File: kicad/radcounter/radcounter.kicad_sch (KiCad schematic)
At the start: 34 parts, among them J1 SiPM(+), J2 SiPM(-), J3 Out, J4 Conn, J5 Conn, J6 Conn, Q2 RUM002N05T2L, T1 ATB322515-0110-T000, U2 MAX9120EXK

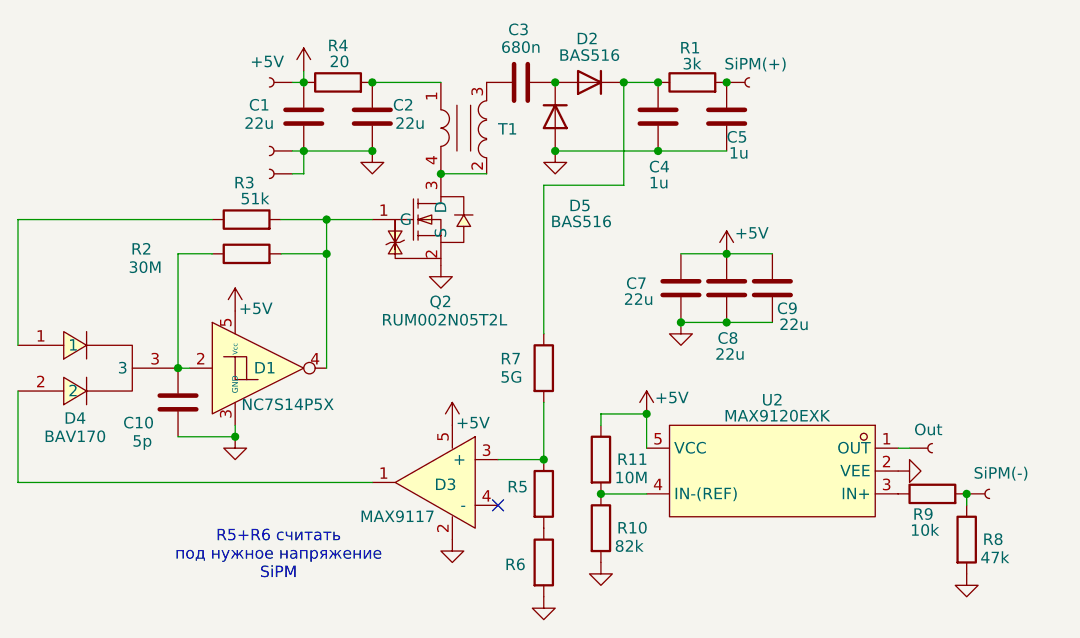
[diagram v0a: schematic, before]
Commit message: удалено:       kicad/radcounter/radcounter-backups/radcounter-2025-12-29_171823.zip 	удалено:       kicad/radcounter/radcounter-backups/radcounter-2026-01-03_121429.zip 	изменено:      kicad/radcounter/radcounter.kicad_pcb 	изменено:      kicad/radcounter/radcounter.kicad_prl 	изменено:      kicad/radcounter/radcounter.kicad_sch
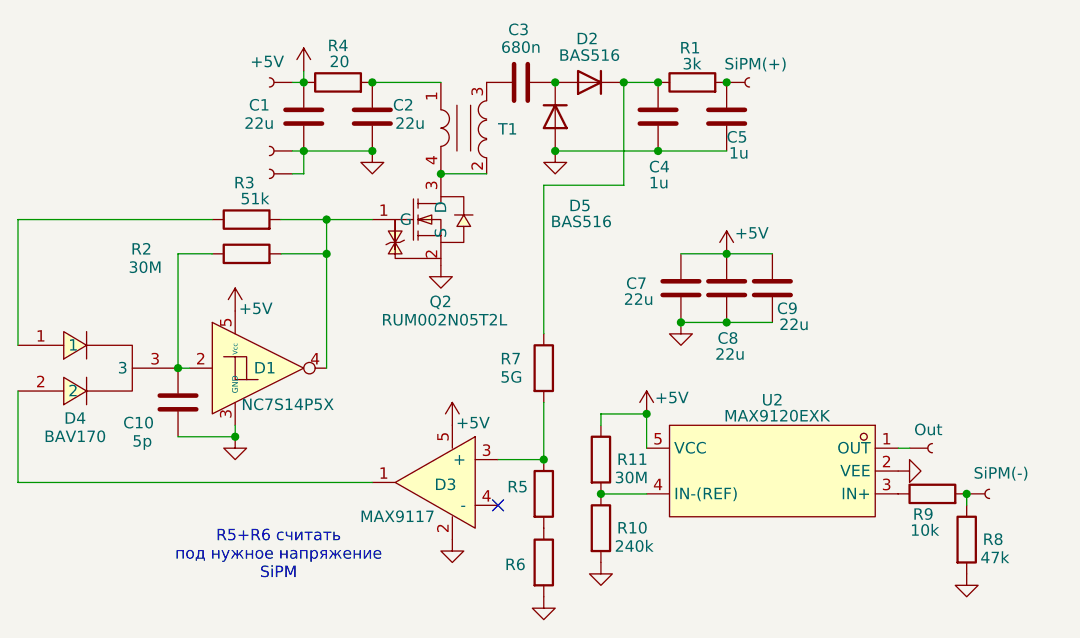
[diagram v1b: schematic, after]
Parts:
- R10: value 82k -> 240k
- R11: value 10M -> 30M
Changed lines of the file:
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@@
 			)
 		)
-		(property "Value" "10M"
+		(property "Value" "30M"
 			(at 164.084 99.822 0)
 			(effects
@@
 			)
 		)
-		(property "Value" "82k"
+		(property "Value" "240k"
 			(at 164.084 107.442 0)
 			(effects
